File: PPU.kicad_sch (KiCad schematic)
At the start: 14 parts, among them U10 74AHC1G04, U4 RP2C02 PPU, U6 74HC573, U7 IS62C256AL-45TLI, U8 SST39SF040-70-4C-NHE

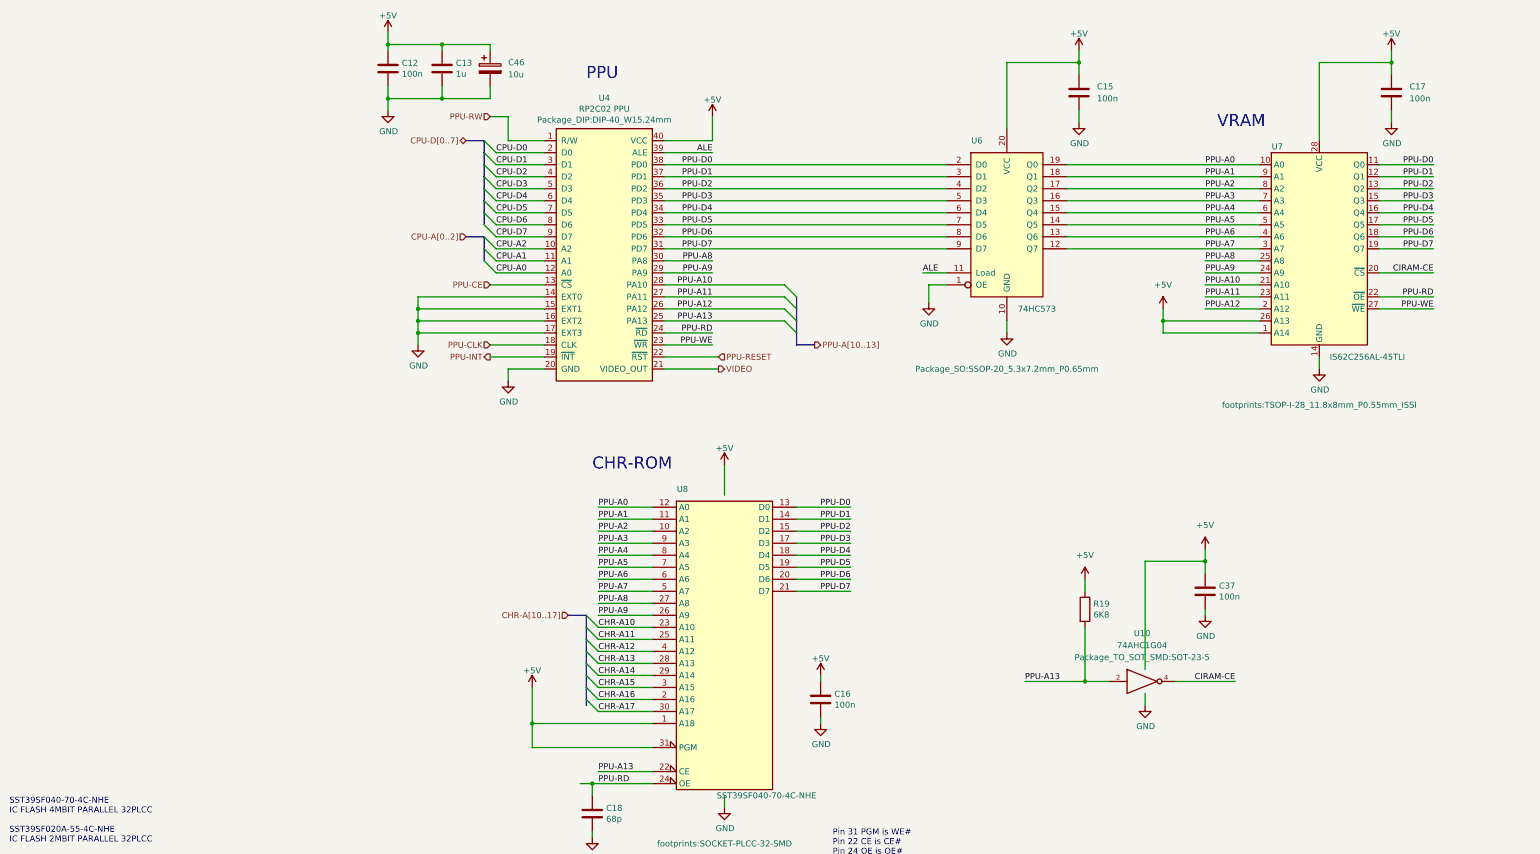
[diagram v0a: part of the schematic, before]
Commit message: rev2 sent to fab
Added CHR RAM.
Changed board to 4 layers (was 2 layers).
Changed passives to 0603 (was 0402)
Fixed CIRAM-A10 not being hooked up
Fixed PPU-A10..A12 being hooked to VRAM but should have been.
Added more silkscreen for easier debugging.
Added filter inductor to 5V from USB-C.
Changed video out to stock (was THS7374)
Changed audio circuit to stock (was headphone amp IC)
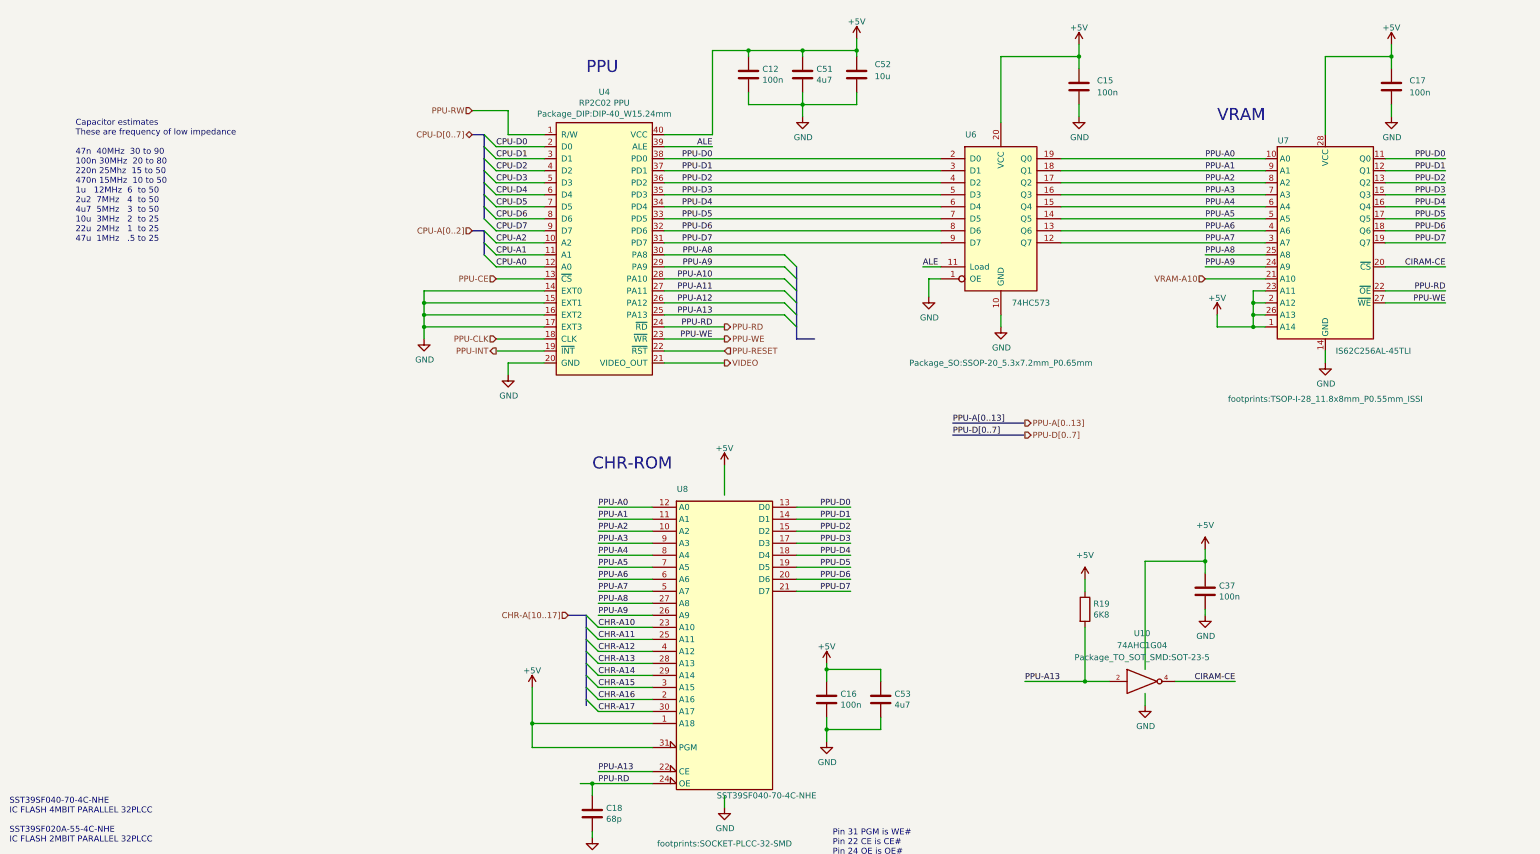
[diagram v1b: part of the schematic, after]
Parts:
- removed C13: 1u, Capacitor_SMD:C_0402_1005Metric, symbol Device:C
- removed C46: 10u, Capacitor_Tantalum_SMD:CP_EIA-3216-18_Kemet-A, symbol Device:C_Polarized
- added C51, C53: 4u7, Capacitor_SMD:C_0805_2012Metric_Pad1.18x1.45mm_HandSolder, symbol Device:C
- added C52: 10u, Capacitor_SMD:C_1206_3216Metric_Pad1.33x1.80mm_HandSolder, symbol Device:C
- C12, C15, C16, C17, C37: footprint Capacitor_SMD:C_0402_1005Metric -> Capacitor_SMD:C_0603_1608Metric_Pad1.08x0.95mm_HandSolder; Digikey 1276-1509-2-ND -> (none); MPN CL05B104KO5NNWC -> (none); QOH 10000 -> (none)
- C18: footprint Capacitor_SMD:C_0402_1005Metric -> Capacitor_SMD:C_0603_1608Metric_Pad1.08x0.95mm_HandSolder; Digikey 311-1340-1-ND -> (none); MPN CC0402JRNPO9BN680 -> (none)
- R19: footprint Resistor_SMD:R_0402_1005Metric -> Resistor_SMD:R_0603_1608Metric_Pad0.98x0.95mm_HandSolder; Digikey 311-6.80KLRCT-ND -> (none); MPN RC0402FR-076K8L -> (none)
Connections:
- net +5V: now also U7.2 (A12), U7.23 (A11), C51.2, C52.1, C53.2
- net GND: now also C51.1, C52.2, C53.1
- net PPU-A10: no longer U7.21 (A10)
- net PPU-A11: no longer U7.23 (A11)
- net PPU-A12: no longer U7.2 (A12)
- new net VRAM-A10: U7.21 (A10)
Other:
- note added: "Capacitor estimates These are frequency of low impedance 47n 40MHz 30 to 90 100n 30MHz 20 to 80 220n 25Mhz 15 to 50 470n 15MHz 10 to 50 1u 12MHz 6 to 50 2u2 7MHz 4 to 50 4u7 5MHz 3 to 50 10u 3MHz 2 to 25 22u 2MHz 1 to 25 47u 1MHz .5 to 25"
- moved on the sheet: C12, C15, C16, C17, U4, U6, U7

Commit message: filled out BOM
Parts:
- C12, C15, C16, C17, C37: Digikey (none) -> 1276-CL10B104KB8WPNDCT-ND; MPN (none) -> CL10B104KB8WPND
- C18: Digikey (none) -> 399-C0603C680J5GAC7867CT-ND; MPN (none) -> C0603C680J5GAC7867
- C51, C53: Digikey (none) -> 1276-1244-1-ND; MPN (none) -> CL21A475KAQNNNE
- C52: Digikey (none) -> 1276-1075-1-ND; MPN (none) -> CL31A106KAHNNNE
- R19: Digikey (none) -> 311-6.80KHRCT-ND; MPN (none) -> RMCF0603FT110RCT-ND
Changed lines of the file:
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@@
   (title_block
     (title "InGame-NES MMC3")
-    (date "2022-06-03")
-    (rev "1")
+    (date "2022-08-02")
+    (rev "2")
     (company "Late to the Game")
   )
@@
       (effects (font (size 1.27 1.27)) hide)
     )
-    (property "Description" "CAP CER 0.1UF 16V X7R 0402" (id 4) (at 93.98 27.94 0)
+    (property "Description" "CAP CER 0.1UF 50V X7R 0603" (id 4) (at 93.98 27.94 0)
       (effects (font (size 1.27 1.27)) hide)
     )
@@
       (effects (font (size 1.27 1.27)) hide)
     )
-    (property "Digikey" "" (id 6) (at 93.98 27.94 0)
-      (effects (font (size 1.27 1.27)) hide)
-    )
-    (property "MPN" "" (id 7) (at 93.98 27.94 0)
+    (property "Digikey" "1276-CL10B104KB8WPNDCT-ND" (id 6) (at 93.98 27.94 0)
+      (effects (font (size 1.27 1.27)) hide)
+    )
+    (property "MPN" "CL10B104KB8WPND" (id 7) (at 93.98 27.94 0)
       (effects (font (size 1.27 1.27)) hide)
     )
@@
       (effects (font (size 1.27 1.27)) hide)
     )
-    (property "Description" "CAP CER 0.1UF 16V X7R 0402" (id 4) (at 163.83 30.48 0)
+    (property "Description" "CAP CER 0.1UF 50V X7R 0603" (id 4) (at 163.83 30.48 0)
       (effects (font (size 1.27 1.27)) hide)
     )
@@
       (effects (font (size 1.27 1.27)) hide)
     )
-    (property "Digikey" "" (id 6) (at 163.83 30.48 0)
-      (effects (font (size 1.27 1.27)) hide)
-    )
-    (property "MPN" "" (id 7) (at 163.83 30.48 0)
+    (property "Digikey" "1276-CL10B104KB8WPNDCT-ND" (id 6) (at 163.83 30.48 0)
+      (effects (font (size 1.27 1.27)) hide)
+    )
+    (property "MPN" "CL10B104KB8WPND" (id 7) (at 163.83 30.48 0)
       (effects (font (size 1.27 1.27)) hide)
     )
@@
       (effects (font (size 1.27 1.27)) hide)
     )
-    (property "Description" "CAP CER 0.1UF 16V X7R 0402" (id 4) (at 229.87 30.48 0)
+    (property "Description" "CAP CER 0.1UF 50V X7R 0603" (id 4) (at 229.87 30.48 0)
       (effects (font (size 1.27 1.27)) hide)
     )
@@
       (effects (font (size 1.27 1.27)) hide)
     )
-    (property "Digikey" "" (id 6) (at 229.87 30.48 0)
-      (effects (font (size 1.27 1.27)) hide)
-    )
-    (property "MPN" "" (id 7) (at 229.87 30.48 0)
+    (property "Digikey" "1276-CL10B104KB8WPNDCT-ND" (id 6) (at 229.87 30.48 0)
+      (effects (font (size 1.27 1.27)) hide)
+    )
+    (property "MPN" "CL10B104KB8WPND" (id 7) (at 229.87 30.48 0)
       (effects (font (size 1.27 1.27)) hide)
     )
@@
       (effects (font (size 1.27 1.27)) hide)
     )
-    (property "Description" "CAP CER 0.1UF 16V X7R 0402" (id 4) (at 110.49 160.02 0)
+    (property "Description" "CAP CER 0.1UF 50V X7R 0603" (id 4) (at 110.49 160.02 0)
       (effects (font (size 1.27 1.27)) hide)
     )
@@
       (effects (font (size 1.27 1.27)) hide)
     )
-    (property "Digikey" "" (id 6) (at 110.49 160.02 0)
-      (effects (font (size 1.27 1.27)) hide)
-    )
-    (property "MPN" "" (id 7) (at 110.49 160.02 0)
+    (property "Digikey" "1276-CL10B104KB8WPNDCT-ND" (id 6) (at 110.49 160.02 0)
+      (effects (font (size 1.27 1.27)) hide)
+    )
+    (property "MPN" "CL10B104KB8WPND" (id 7) (at 110.49 160.02 0)
       (effects (font (size 1.27 1.27)) hide)
     )
@@
       (effects (font (size 1.27 1.27)) hide)
     )
-    (property "Digikey" "" (id 5) (at 60.96 184.15 0)
-      (effects (font (size 1.27 1.27)) hide)
-    )
-    (property "MPN" "" (id 6) (at 60.96 184.15 0)
+    (property "Digikey" "399-C0603C680J5GAC7867CT-ND" (id 5) (at 60.96 184.15 0)
+      (effects (font (size 1.27 1.27)) hide)
+    )
+    (property "MPN" "C0603C680J5GAC7867" (id 6) (at 60.96 184.15 0)
       (effects (font (size 1.27 1.27)) hide)
     )
@@
       (effects (font (size 1.27 1.27)) hide)
     )
-    (property "Description" "RES 6.8K OHM" (id 4) (at 165.1 140.97 0)
-      (effects (font (size 1.27 1.27)) hide)
-    )
-    (property "Digikey" "" (id 5) (at 165.1 140.97 0)
-      (effects (font (size 1.27 1.27)) hide)
-    )
-    (property "MPN" "" (id 6) (at 165.1 140.97 0)
+    (property "Description" "RES SMD 6.8K OHM 1% 1/10W 0603" (id 4) (at 165.1 140.97 0)
+      (effects (font (size 1.27 1.27)) hide)
+    )
+    (property "Digikey" "311-6.80KHRCT-ND" (id 5) (at 165.1 140.97 0)
+      (effects (font (size 1.27 1.27)) hide)
+    )
+    (property "MPN" "RMCF0603FT110RCT-ND" (id 6) (at 165.1 140.97 0)
       (effects (font (size 1.27 1.27)) hide)
     )
@@
       (effects (font (size 1.27 1.27)) hide)
     )
-    (property "Description" "CAP CER 0.1UF 16V X7R 0402" (id 4) (at 190.5 137.16 0)
+    (property "Description" "CAP CER 0.1UF 50V X7R 0603" (id 4) (at 190.5 137.16 0)
       (effects (font (size 1.27 1.27)) hide)
     )
@@
       (effects (font (size 1.27 1.27)) hide)
     )
-    (property "Digikey" "" (id 6) (at 190.5 137.16 0)
-      (effects (font (size 1.27 1.27)) hide)
-    )
-    (property "MPN" "" (id 7) (at 190.5 137.16 0)
+    (property "Digikey" "1276-CL10B104KB8WPNDCT-ND" (id 6) (at 190.5 137.16 0)
+      (effects (font (size 1.27 1.27)) hide)
+    )
+    (property "MPN" "CL10B104KB8WPND" (id 7) (at 190.5 137.16 0)
       (effects (font (size 1.27 1.27)) hide)
     )
@@
       (effects (font (size 1.27 1.27)) hide)
     )
-    (property "Description" "CAP CER 10UF 10V X5R 0805" (id 4) (at 116.84 27.94 0)
+    (property "Description" "CAP CER 10UF 25V X5R 1206" (id 4) (at 116.84 27.94 0)
       (effects (font (size 1.27 1.27)) hide)
     )
@@
       (effects (font (size 1.27 1.27)) hide)
     )
-    (property "Digikey" "" (id 6) (at 116.84 27.94 0)
-      (effects (font (size 1.27 1.27)) hide)
-    )
-    (property "MPN" "" (id 7) (at 116.84 27.94 0)
+    (property "Digikey" "1276-1075-1-ND" (id 6) (at 116.84 27.94 0)
+      (effects (font (size 1.27 1.27)) hide)
+    )
+    (property "MPN" "CL31A106KAHNNNE" (id 7) (at 116.84 27.94 0)
       (effects (font (size 1.27 1.27)) hide)
     )
@@
       (effects (font (size 1.27 1.27)) hide)
     )
-    (property "Description" "" (id 4) (at 105.41 27.94 0)
+    (property "Description" "CAP CER 4.7UF 25V X5R 0805" (id 4) (at 105.41 27.94 0)
       (effects (font (size 1.27 1.27)) hide)
     )
@@
       (effects (font (size 1.27 1.27)) hide)
     )
-    (property "Digikey" "" (id 6) (at 105.41 27.94 0)
-      (effects (font (size 1.27 1.27)) hide)
-    )
-    (property "MPN" "" (id 7) (at 105.41 27.94 0)
+    (property "Digikey" "1276-1244-1-ND" (id 6) (at 105.41 27.94 0)
+      (effects (font (size 1.27 1.27)) hide)
+    )
+    (property "MPN" "CL21A475KAQNNNE" (id 7) (at 105.41 27.94 0)
       (effects (font (size 1.27 1.27)) hide)
     )
@@
       (effects (font (size 1.27 1.27)) hide)
     )
-    (property "Description" "" (id 4) (at 121.92 160.02 0)
+    (property "Description" "CAP CER 4.7UF 25V X5R 0805" (id 4) (at 121.92 160.02 0)
       (effects (font (size 1.27 1.27)) hide)
     )
@@
       (effects (font (size 1.27 1.27)) hide)
     )
-    (property "Digikey" "" (id 6) (at 121.92 160.02 0)
-      (effects (font (size 1.27 1.27)) hide)
-    )
-    (property "MPN" "" (id 7) (at 121.92 160.02 0)
-      (effects (font (size 1.27 1.27)) hide)
-    )
+    (property "Digikey" "1276-1244-1-ND" (id 6) (at 121.92 160.02 0)
+      (effects (font (size 1.27 1.27)) hide)
+    )
+    (property "MPN" "CL21A475KAQNNNE" (id 7) (at 121.92 160.02 0)
+      (effects (font (size 1.27 1.27)) hide)
+    )
